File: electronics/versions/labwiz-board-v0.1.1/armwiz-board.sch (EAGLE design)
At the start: 99 parts, among them J1 MICRO-SDCARD-CONNECTOR-330006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, J15 Cortex Debug, J16 ST-Link v2, J2 CORTEX_DEBUGSMD, U1 STM32F10XRXT6, U4 MIC5219-3.3V, X1 FH12-12S-1S, Y3 32.768kHz

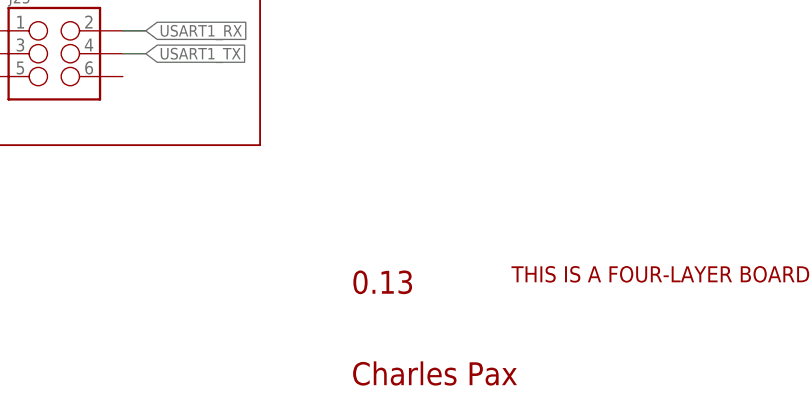
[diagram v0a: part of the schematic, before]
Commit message: Added a header for USART1 Rx Tx.
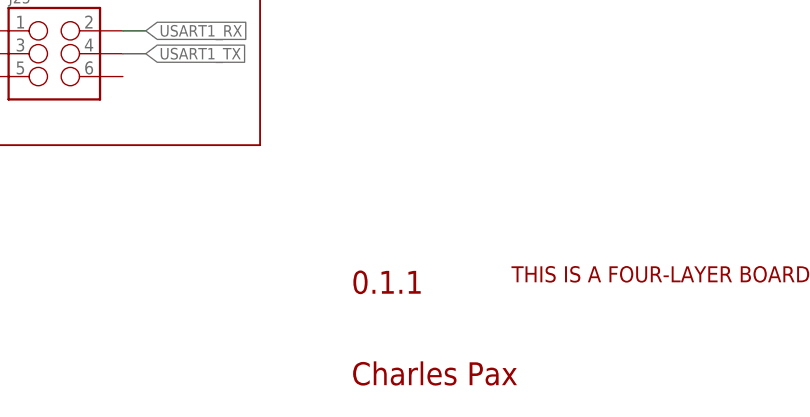
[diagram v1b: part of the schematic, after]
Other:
- note added: "0.1.1"
- note removed: "0.13"
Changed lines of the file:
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@@
 <wire x1="116.84" y1="101.6" x2="116.84" y2="142.24" width="0.2032" layer="94"/>
 <text x="119.38" y="137.16" size="3.81" layer="94">Buttons</text>
-<text x="330.2" y="15.24" size="2.54" layer="94" align="center-left">0.13</text>
+<text x="330.2" y="15.24" size="2.54" layer="94" align="center-left">0.1.1</text>
 <wire x1="116.84" y1="193.04" x2="185.42" y2="193.04" width="0.2032" layer="94"/>
 <wire x1="116.84" y1="193.04" x2="116.84" y2="144.78" width="0.2032" layer="94"/>
